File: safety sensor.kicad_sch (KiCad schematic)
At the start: 29 parts, among them IC1 STM8S003F3P6, J1 Conn_01x02, J2 SDA, J3 SCL, J4 INT, J5 Conn_01x02, J6 SWIM, U1 LD1117V33, U2 VCNL3020-GS08

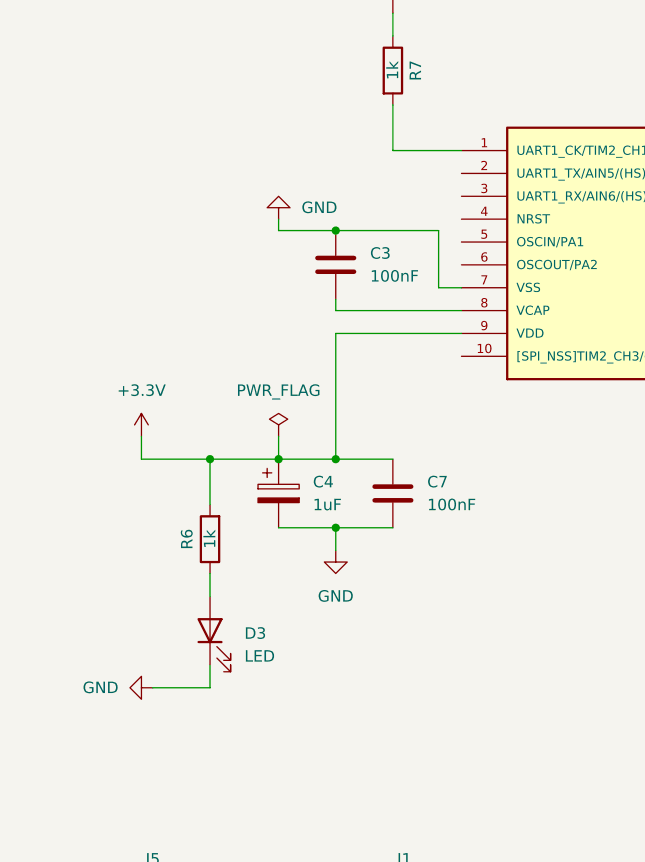
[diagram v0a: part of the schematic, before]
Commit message: add pull up resistor for nrst, change hole size for voltage connectors
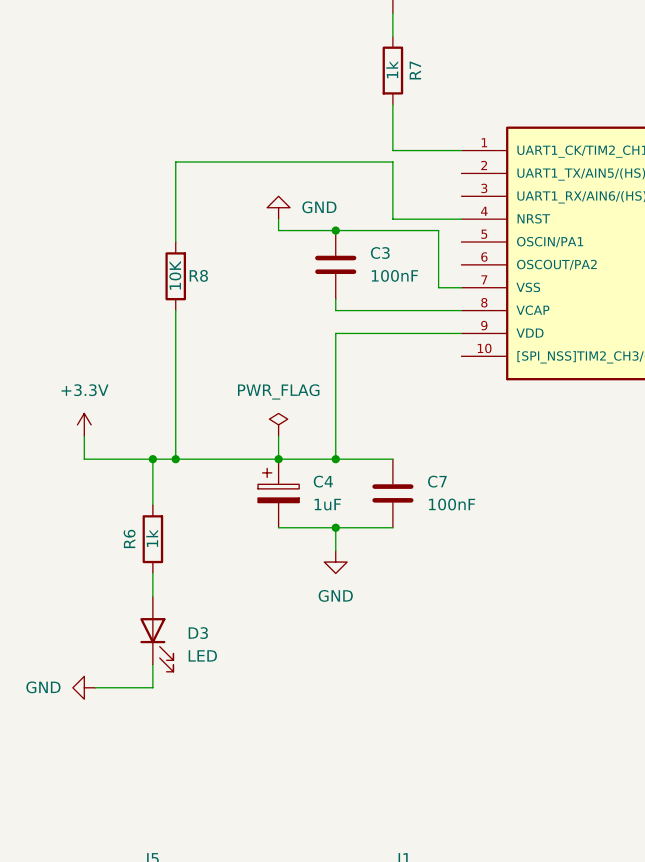
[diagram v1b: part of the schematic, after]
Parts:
- added R8: 10K, Resistor_THT:R_Axial_DIN0207_L6.3mm_D2.5mm_P10.16mm_Horizontal, symbol Device:R
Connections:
- net +3.3V: now also R8.1
- net at IC1.4 (NRST): now also R8.2
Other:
- moved on the sheet: D3, R6
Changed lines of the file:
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@@
   (junction (at 156.21 146.05) (diameter 0) (color 0 0 0 0)
   )
-  (junction (at 33.02 115.57) (diameter 0) (color 0 0 0 0)
+  (junction (at 26.67 115.57) (diameter 0) (color 0 0 0 0)
   )
   (junction (at 114.3 146.05) (diameter 0) (color 0 0 0 0)
@@
   )
   (junction (at 168.91 76.2) (diameter 0) (color 0 0 0 0)
+  )
+  (junction (at 29.21 115.57) (diameter 0) (color 0 0 0 0)
   )
   (junction (at 40.64 115.57) (diameter 0) (color 0 0 0 0)
@@
     (stroke (width 0) (type default) (color 0 0 0 0))
   )
-  (wire (pts (xy 33.02 140.97) (xy 26.67 140.97))
+  (wire (pts (xy 26.67 140.97) (xy 20.32 140.97))
     (stroke (width 0) (type default) (color 0 0 0 0))
   )
@@
     (stroke (width 0) (type default) (color 0 0 0 0))
   )
-  (wire (pts (xy 33.02 128.27) (xy 33.02 130.81))
+  (wire (pts (xy 26.67 128.27) (xy 26.67 130.81))
     (stroke (width 0) (type default) (color 0 0 0 0))
   )
@@
     (stroke (width 0) (type default) (color 0 0 0 0))
   )
-  (wire (pts (xy 33.02 138.43) (xy 33.02 140.97))
+  (wire (pts (xy 26.67 138.43) (xy 26.67 140.97))
     (stroke (width 0) (type default) (color 0 0 0 0))
   )
@@
     (stroke (width 0) (type default) (color 0 0 0 0))
   )
-  (wire (pts (xy 33.02 115.57) (xy 33.02 120.65))
+  (wire (pts (xy 26.67 115.57) (xy 26.67 120.65))
     (stroke (width 0) (type default) (color 0 0 0 0))
   )
@@
     (stroke (width 0) (type default) (color 0 0 0 0))
   )
-  (wire (pts (xy 25.4 113.03) (xy 25.4 115.57))
+  (wire (pts (xy 19.05 113.03) (xy 19.05 115.57))
     (stroke (width 0) (type default) (color 0 0 0 0))
   )
@@
     (stroke (width 0) (type default) (color 0 0 0 0))
   )
-  (wire (pts (xy 33.02 115.57) (xy 40.64 115.57))
-    (stroke (width 0) (type default) (color 0 0 0 0))
-  )
   (wire (pts (xy 161.29 146.05) (xy 162.56 146.05))
     (stroke (width 0) (type default) (color 0 0 0 0))
@@
     (stroke (width 0) (type default) (color 0 0 0 0))
   )
-  (wire (pts (xy 25.4 115.57) (xy 33.02 115.57))
+  (wire (pts (xy 19.05 115.57) (xy 26.67 115.57))
     (stroke (width 0) (type default) (color 0 0 0 0))
   )
@@
     (stroke (width 0) (type default) (color 0 0 0 0))
   )
+  (wire (pts (xy 29.21 115.57) (xy 40.64 115.57))
+    (stroke (width 0) (type default) (color 0 0 0 0))
+  )
   (wire (pts (xy 31.75 176.53) (xy 35.56 176.53))
     (stroke (width 0) (type default) (color 0 0 0 0))
@@
     (stroke (width 0) (type default) (color 0 0 0 0))
   )
+  (wire (pts (xy 53.34 82.55) (xy 53.34 88.9))
+    (stroke (width 0) (type default) (color 0 0 0 0))
+  )
+  (wire (pts (xy 60.96 88.9) (xy 53.34 88.9))
+    (stroke (width 0) (type default) (color 0 0 0 0))
+  )
   (wire (pts (xy 153.67 71.12) (xy 200.66 71.12))
     (stroke (width 0) (type default) (color 0 0 0 0))
@@
     (stroke (width 0) (type default) (color 0 0 0 0))
   )
+  (wire (pts (xy 29.21 115.57) (xy 26.67 115.57))
+    (stroke (width 0) (type default) (color 0 0 0 0))
+  )
   (wire (pts (xy 149.86 99.06) (xy 153.67 99.06))
     (stroke (width 0) (type default) (color 0 0 0 0))
   )
+  (wire (pts (xy 29.21 99.06) (xy 29.21 115.57))
+    (stroke (width 0) (type default) (color 0 0 0 0))
+  )
   (wire (pts (xy 170.18 36.83) (xy 186.69 36.83))
     (stroke (width 0) (type default) (color 0 0 0 0))
@@
     (stroke (width 0) (type default) (color 0 0 0 0))
   )
+  (wire (pts (xy 29.21 82.55) (xy 53.34 82.55))
+    (stroke (width 0) (type default) (color 0 0 0 0))
+  )
   (wire (pts (xy 114.3 162.56) (xy 130.81 162.56))
+    (stroke (width 0) (type default) (color 0 0 0 0))
+  )
+  (wire (pts (xy 29.21 91.44) (xy 29.21 82.55))
     (stroke (width 0) (type default) (color 0 0 0 0))
   )
@@
     (pin "1")
   )
-  (symbol (lib_id "power:+3.3V") (at 25.4 113.03 0) (unit 1)
-    (in_bom yes) (on_board yes) (fields_autoplaced)
-    (property "Reference" "#PWR0114" (id 0) (at 25.4 116.84 0)
-      (effects (font (size 1.27 1.27)) hide)
-    )
-    (property "Value" "+3.3V" (id 1) (at 25.4 107.95 0))
-    (property "Footprint" "" (id 2) (at 25.4 113.03 0)
-      (effects (font (size 1.27 1.27)) hide)
-    )
-    (property "Datasheet" "" (id 3) (at 25.4 113.03 0)
+  (symbol (lib_id "power:+3.3V") (at 19.05 113.03 0) (unit 1)
+    (in_bom yes) (on_board yes) (fields_autoplaced)
+    (property "Reference" "#PWR0114" (id 0) (at 19.05 116.84 0)
+      (effects (font (size 1.27 1.27)) hide)
+    )
+    (property "Value" "+3.3V" (id 1) (at 19.05 107.95 0))
+    (property "Footprint" "" (id 2) (at 19.05 113.03 0)
+      (effects (font (size 1.27 1.27)) hide)
+    )
+    (property "Datasheet" "" (id 3) (at 19.05 113.03 0)
       (effects (font (size 1.27 1.27)) hide)
     )
@@
     (pin "2")
   )
-  (symbol (lib_id "Device:LED") (at 33.02 134.62 90) (unit 1)
-    (in_bom yes) (on_board yes) (fields_autoplaced)
-    (property "Reference" "D3" (id 0) (at 36.83 134.9374 90)
+  (symbol (lib_id "Device:LED") (at 26.67 134.62 90) (unit 1)
+    (in_bom yes) (on_board yes) (fields_autoplaced)
+    (property "Reference" "D3" (id 0) (at 30.48 134.9374 90)
       (effects (font (size 1.27 1.27)) (justify right))
     )
-    (property "Value" "LED" (id 1) (at 36.83 137.4774 90)
+    (property "Value" "LED" (id 1) (at 30.48 137.4774 90)
       (effects (font (size 1.27 1.27)) (justify right))
     )
-    (property "Footprint" "LED_THT:LED_D5.0mm" (id 2) (at 33.02 134.62 0)
-      (effects (font (size 1.27 1.27)) hide)
-    )
-    (property "Datasheet" "~" (id 3) (at 33.02 134.62 0)
-      (effects (font (size 1.27 1.27)) hide)
-    )
-    (pin "1")
-    (pin "2")
-  )
-  (symbol (lib_id "Device:R") (at 33.02 124.46 180) (unit 1)
-    (in_bom yes) (on_board yes)
-    (property "Reference" "R6" (id 0) (at 30.48 124.46 90))
-    (property "Value" "1k" (id 1) (at 33.02 124.46 90))
-    (property "Footprint" "Resistor_THT:R_Axial_DIN0207_L6.3mm_D2.5mm_P10.16mm_Horizontal" (id 2) (at 34.798 124.46 90)
-      (effects (font (size 1.27 1.27)) hide)
-    )
-    (property "Datasheet" "~" (id 3) (at 33.02 124.46 0)
+    (property "Footprint" "LED_THT:LED_D5.0mm" (id 2) (at 26.67 134.62 0)
+      (effects (font (size 1.27 1.27)) hide)
+    )
+    (property "Datasheet" "~" (id 3) (at 26.67 134.62 0)
+      (effects (font (size 1.27 1.27)) hide)
+    )
+    (pin "1")
+    (pin "2")
+  )
+  (symbol (lib_id "Device:R") (at 26.67 124.46 180) (unit 1)
+    (in_bom yes) (on_board yes)
+    (property "Reference" "R6" (id 0) (at 24.13 124.46 90))
+    (property "Value" "1k" (id 1) (at 26.67 124.46 90))
+    (property "Footprint" "Resistor_THT:R_Axial_DIN0207_L6.3mm_D2.5mm_P10.16mm_Horizontal" (id 2) (at 28.448 124.46 90)
+      (effects (font (size 1.27 1.27)) hide)
+    )
+    (property "Datasheet" "~" (id 3) (at 26.67 124.46 0)
       (effects (font (size 1.27 1.27)) hide)
     )
@@
     (pin "1")
   )
-  (symbol (lib_id "power:GND") (at 26.67 140.97 270) (unit 1)
-    (in_bom yes) (on_board yes) (fields_autoplaced)
-    (property "Reference" "#PWR0116" (id 0) (at 20.32 140.97 0)
-      (effects (font (size 1.27 1.27)) hide)
-    )
-    (property "Value" "GND" (id 1) (at 22.86 140.9701 90)
+  (symbol (lib_id "power:GND") (at 20.32 140.97 270) (unit 1)
+    (in_bom yes) (on_board yes) (fields_autoplaced)
+    (property "Reference" "#PWR0116" (id 0) (at 13.97 140.97 0)
+      (effects (font (size 1.27 1.27)) hide)
+    )
+    (property "Value" "GND" (id 1) (at 16.51 140.9701 90)
       (effects (font (size 1.27 1.27)) (justify right))
     )
-    (property "Footprint" "" (id 2) (at 26.67 140.97 0)
-      (effects (font (size 1.27 1.27)) hide)
-    )
-    (property "Datasheet" "" (id 3) (at 26.67 140.97 0)
+    (property "Footprint" "" (id 2) (at 20.32 140.97 0)
+      (effects (font (size 1.27 1.27)) hide)
+    )
+    (property "Datasheet" "" (id 3) (at 20.32 140.97 0)
       (effects (font (size 1.27 1.27)) hide)
     )
@@
     )
     (pin "1")
+  )
+  (symbol (lib_id "Device:R") (at 29.21 95.25 180) (unit 1)
+    (in_bom yes) (on_board yes)
+    (property "Reference" "R8" (id 0) (at 31.75 95.25 0))
+    (property "Value" "10K" (id 1) (at 29.21 95.25 90))
+    (property "Footprint" "Resistor_THT:R_Axial_DIN0207_L6.3mm_D2.5mm_P10.16mm_Horizontal" (id 2) (at 30.988 95.25 90)
+      (effects (font (size 1.27 1.27)) hide)
+    )
+    (property "Datasheet" "~" (id 3) (at 29.21 95.25 0)
+      (effects (font (size 1.27 1.27)) hide)
+    )
+    (pin "1")
+    (pin "2")
   )
   (sheet_instances
@@
       (reference "R7") (unit 1) (value "1k") (footprint "Resistor_THT:R_Axial_DIN0207_L6.3mm_D2.5mm_P10.16mm_Horizontal")
     )
+    (path "/f702d323-ff1f-4f7b-a8df-451616e1a819"
+      (reference "R8") (unit 1) (value "10K") (footprint "Resistor_THT:R_Axial_DIN0207_L6.3mm_D2.5mm_P10.16mm_Horizontal")
+    )
     (path "/c6744e4c-2e81-4a40-98f6-86be5ebb208f"
